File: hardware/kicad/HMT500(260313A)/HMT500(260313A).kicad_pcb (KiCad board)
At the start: 4 copper layers, 56.5 x 23 mm, 110 parts, among them J1 SM08B-GHS-TB, J2 TC2030-IDC-NL, J3 SM04B-SRSS-TB, J5 CHASSIS wire, U1 TPS26600PWPR, U10 TPS26611DDFR, U11 THVD2410DGKR, U12 OPA197IDBVR, U13 OPA197IDBVR, U14 SN74LVC2G32DCUR, U15 LMR51606YFDBVR, U2 LMR51606YFDBVR, U3 TPS7A2033PDBVR, U4 STM32G0B1CCT6, U5 PCAP04-AQFM-24, U6 ADS1220IPWR, U7 DAC8760IPWP, U8 DAC8760IPWP, U9 TPS26611DDFR

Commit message: 회로 v0.10: AO D30/D40을 TVS1401 14 V로 변경
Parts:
- D30, D40: value TVS3301DRBR -> TVS1401DRBR

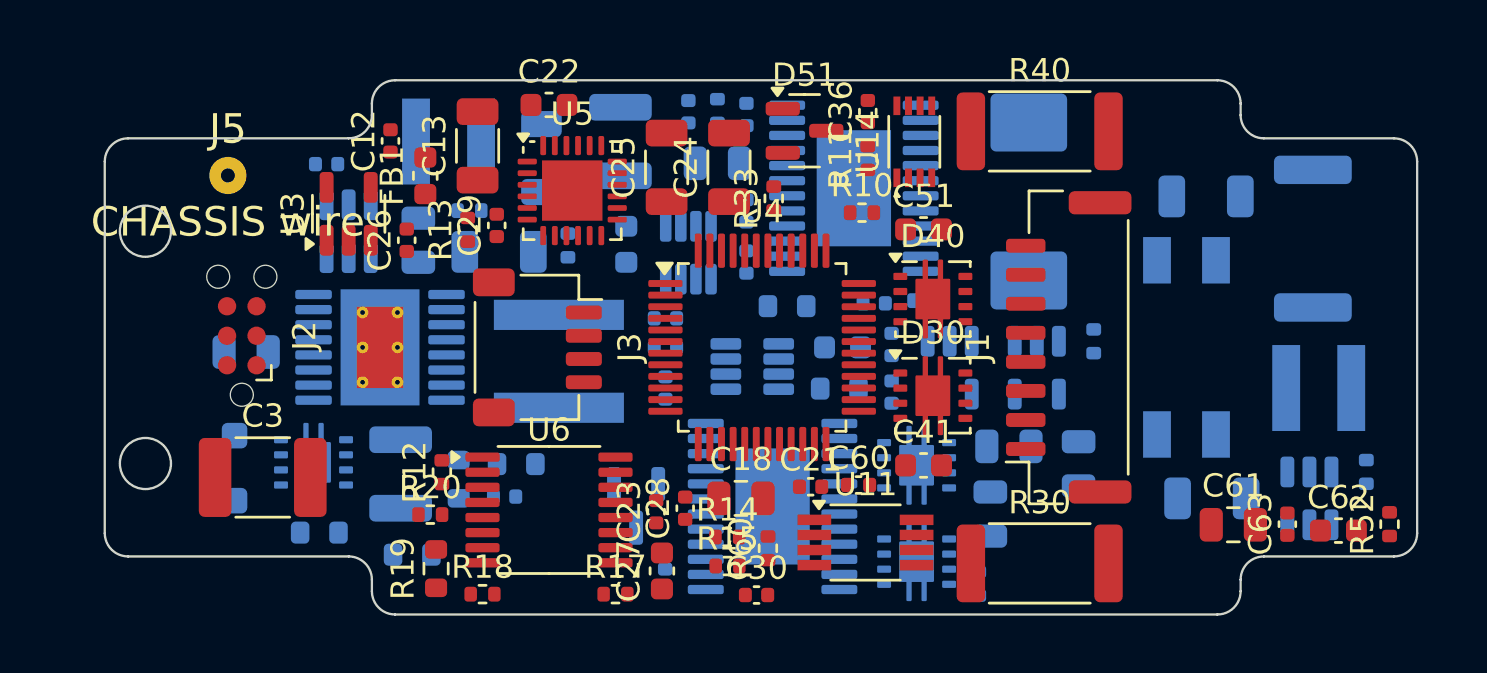
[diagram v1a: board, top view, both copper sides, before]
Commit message: Add HMT500 A1 routing draft and correct SMNR4020 land patterns
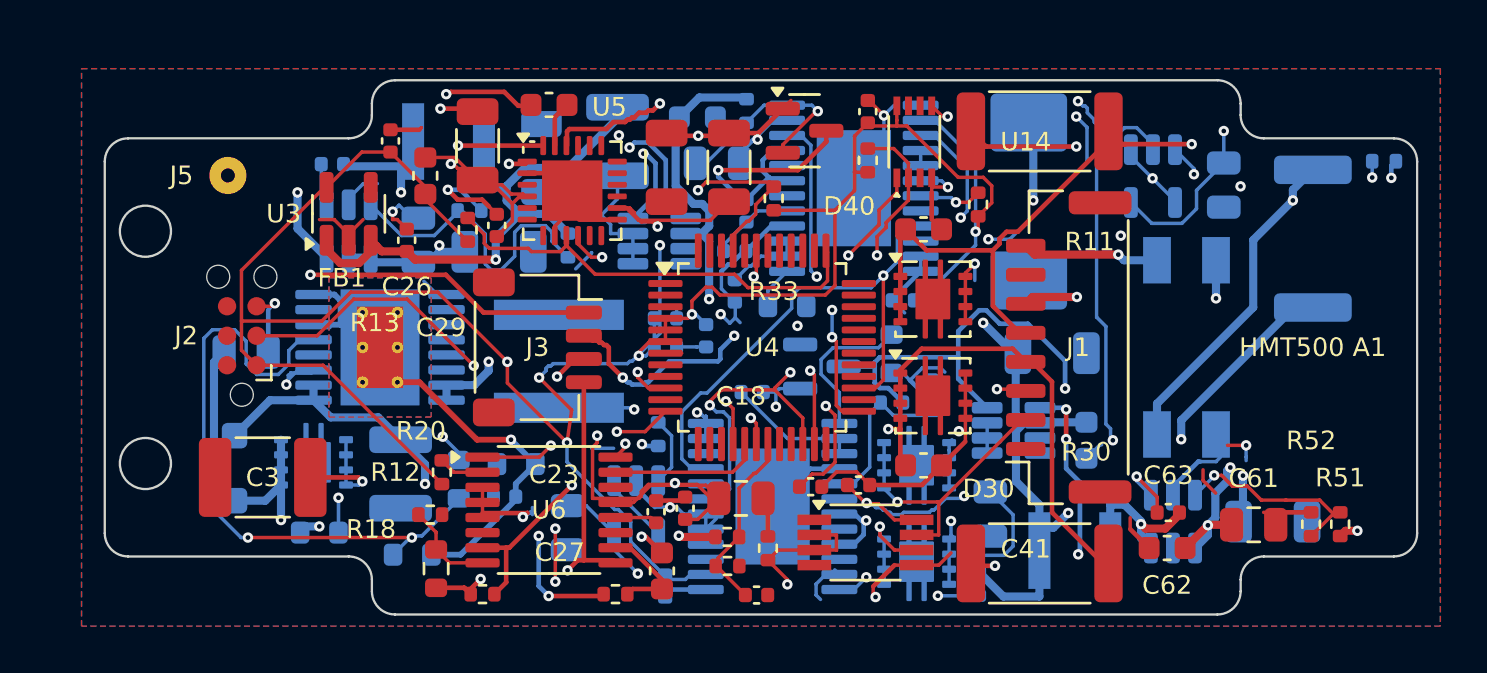
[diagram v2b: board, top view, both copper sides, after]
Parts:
- C1, C16, C18, C42, C45, C52, C55, C61: footprint Capacitor_SMD:C_0805_2012Metric -> HMT500_260313A:C_0805_2012Metric
- C12, C14, C15, C20, C21, C23, C26, C28, C29, C30, C36, C4, C40, C44, C47, C48, C50, C54, C57, C58, C60, C63, C8: footprint Capacitor_SMD:C_0402_1005Metric -> HMT500_260313A:C_0402_1005Metric
- C13, C24, C25, C5, C64, C65: footprint Capacitor_SMD:C_1206_3216Metric -> HMT500_260313A:C_1206_3216Metric
- C2, C6: footprint Capacitor_SMD:C_1210_3225Metric -> HMT500_260313A:C_1210_3225Metric
- C22, C27, C41, C46, C51, C56, C62: footprint Capacitor_SMD:C_0603_1608Metric -> HMT500_260313A:C_0603_1608Metric
- C3: footprint Capacitor_SMD:C_1812_4532Metric -> HMT500_260313A:C_1812_4532Metric
- D1: footprint Diode_SMD:D_SMC -> HMT500_260313A:D_SMC
- D3: footprint Diode_SMD:D_SOD-123F -> HMT500_260313A:D_SOD-123F
- D41, D51: footprint Package_TO_SOT_SMD:SOT-23 -> HMT500_260313A:SOT-23
- FB1: footprint Inductor_SMD:L_0603_1608Metric -> HMT500_260313A:L_0603_1608Metric
- J1: footprint Connector_JST:JST_GH_SM08B-GHS-TB_1x08-1MP_P1.25mm_Horizontal -> HMT500_260313A:JST_GH_SM08B-GHS-TB_1x08-1MP_P1.25mm_Horizontal
- J2: footprint Connector:Tag-Connect_TC2030-IDC-NL_2x03_P1.27mm_Vertical -> HMT500_260313A:Tag-Connect_TC2030-IDC-NL_2x03_P1.27mm_Vertical
- J3: footprint Connector_JST:JST_SH_SM04B-SRSS-TB_1x04-1MP_P1.00mm_Horizontal -> HMT500_260313A:JST_SH_SM04B-SRSS-TB_1x04-1MP_P1.00mm_Horizontal
- L1: footprint Inductor_SMD:L_CommonMode_Wuerth_WE-SL2 -> HMT500_260313A:L_CommonMode_Wuerth_WE-SL2
- L2, L3: footprint Inductor_SMD:L_Taiyo-Yuden_NR-40xx -> HMT500_260313A:L_SXN_SMNR4020
- R1, R30, R40: footprint Resistor_SMD:R_2512_6332Metric -> HMT500_260313A:R_2512_6332Metric
- R10, R11, R12, R13, R14, R15, R17, R18, R20, R31, R33, R34, R41, R44, R52, R60, R8, R9: footprint Resistor_SMD:R_0402_1005Metric -> HMT500_260313A:R_0402_1005Metric
- R19, R3, R32, R4, R42, R5, R6: footprint Resistor_SMD:R_0603_1608Metric -> HMT500_260313A:R_0603_1608Metric
- R2: footprint Resistor_SMD:R_1206_3216Metric -> HMT500_260313A:R_1206_3216Metric
- R51: footprint Resistor_SMD:R_0402_1005Metric -> HMT500_260313A:R_0402_1005Metric; moved to F.Cu
- U1: footprint Package_SO:HTSSOP-16-1EP_4.4x5mm_P0.65mm_EP3.4x5mm_Mask2.46x2.31mm_ThermalVias -> HMT500_260313A:HTSSOP-16-1EP_4.4x5mm_P0.65mm_EP3.4x5mm_Mask2.46x2.31mm_ThermalVias
- U10, U9: footprint Package_TO_SOT_SMD:SOT-23-8 -> HMT500_260313A:SOT-23-8
- U11: footprint Package_SO:VSSOP-8_3.0x3.0mm_P0.65mm -> HMT500_260313A:VSSOP-8_3.0x3.0mm_P0.65mm
- U12, U13, U3: footprint Package_TO_SOT_SMD:SOT-23-5 -> HMT500_260313A:SOT-23-5
- U14: footprint Package_SO:VSSOP-8_2.3x2mm_P0.5mm -> HMT500_260313A:VSSOP-8_2.3x2mm_P0.5mm
- U15, U2: footprint Package_TO_SOT_SMD:SOT-23-6 -> HMT500_260313A:SOT-23-6
- U4: footprint Package_QFP:LQFP-48_7x7mm_P0.5mm -> HMT500_260313A:LQFP-48_7x7mm_P0.5mm
- U5: footprint Package_DFN_QFN:QFN-24-1EP_4x4mm_P0.5mm_EP2.6x2.6mm -> HMT500_260313A:QFN-24-1EP_4x4mm_P0.5mm_EP2.6x2.6mm
- U6: footprint Package_SO:TSSOP-16_4.4x5mm_P0.65mm -> HMT500_260313A:TSSOP-16_4.4x5mm_P0.65mm
- U7, U8: footprint Package_SO:HTSSOP-24-1EP_4.4x7.8mm_P0.65mm_EP3.2x5mm -> HMT500_260313A:HTSSOP-24-1EP_4.4x7.8mm_P0.65mm_EP3.2x5mm
- moved C45 19.3 mm to (119.9, 107.8), turned to -90 degrees
- moved U12 14.8 mm to (122.9, 106.9)
- moved R41 14.7 mm to (155.1, 92.0), turned to 0 degrees
- moved C55 13.5 mm to (148.2, 93.0)
- moved R31 12.9 mm to (123.8, 103.7), turned to -90 degrees
- moved L3 12.6 mm to (141.8, 108.8), turned to 180 degrees
- moved U9 11.6 mm to (139.1, 103.6)
- moved C46 11.2 mm to (142.3, 104.0), turned to -90 degrees
- moved C54 10.5 mm to (134.4, 98.0), turned to 180 degrees
- moved D41 10.0 mm to (130.9, 100.8), turned to 0 degrees
- moved U13 9.65 mm to (145.1, 92.6)
- moved C65 9.46 mm to (140.8, 100.2)
- moved C62 7.41 mm to (145.7, 108.6), turned to 180 degrees
- moved C58 6.32 mm to (127.1, 95.9), turned to 0 degrees
- moved C56 6.26 mm to (125.5, 90.1), turned to 0 degrees
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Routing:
- net +3V3: track 0.00 -> 200.0 mm, vias 0 -> 13
- net GND: track 0.00 -> 145.7 mm, vias 0 -> 24
- net VIN_P: track 0.00 -> 71.2 mm, vias 0 -> 5
- net VIN_F: track 0.00 -> 62.9 mm, vias 0 -> 2
- net VAO: track 0.00 -> 62.6 mm, vias 0 -> 5
- net DAC1_LATCH: track 0.00 -> 35.1 mm, vias 0 -> 3
- net OUT2_EXT: track 0.00 -> 34.0 mm, vias 0 -> 2
- net DAC2_AVDD: track 0.00 -> 34.0 mm, vias 0 -> 2
- net RS485_DE: track 0.00 -> 33.9 mm, vias 0 -> 4
- net NRST: track 0.00 -> 33.5 mm, vias 0 -> 3
- net DAC1_OUT: track 0.00 -> 33.2 mm, vias 0 -> 2
- net OUT1_EXT: track 0.00 -> 32.8 mm, vias 0 -> 2
- net DAC_SCK: track 0.00 -> 32.6 mm, vias 0 -> 6
- net +3V3A: track 0.00 -> 30.7 mm, vias 0 -> 2
- net OUT2_P: track 0.00 -> 30.3 mm, vias 0 -> 2
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- added copper zone on B.Cu, net EF_RTN
- added copper zone on F.Cu, net EF_RTN
- added copper zone on B.Cu, net GND
- added copper zone on F.Cu, net GND
- added copper zone on In1.Cu, net GND
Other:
- board text added: "HMT500 A1"

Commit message: Save HMT500 A2 layout improvements as an incomplete routing draft
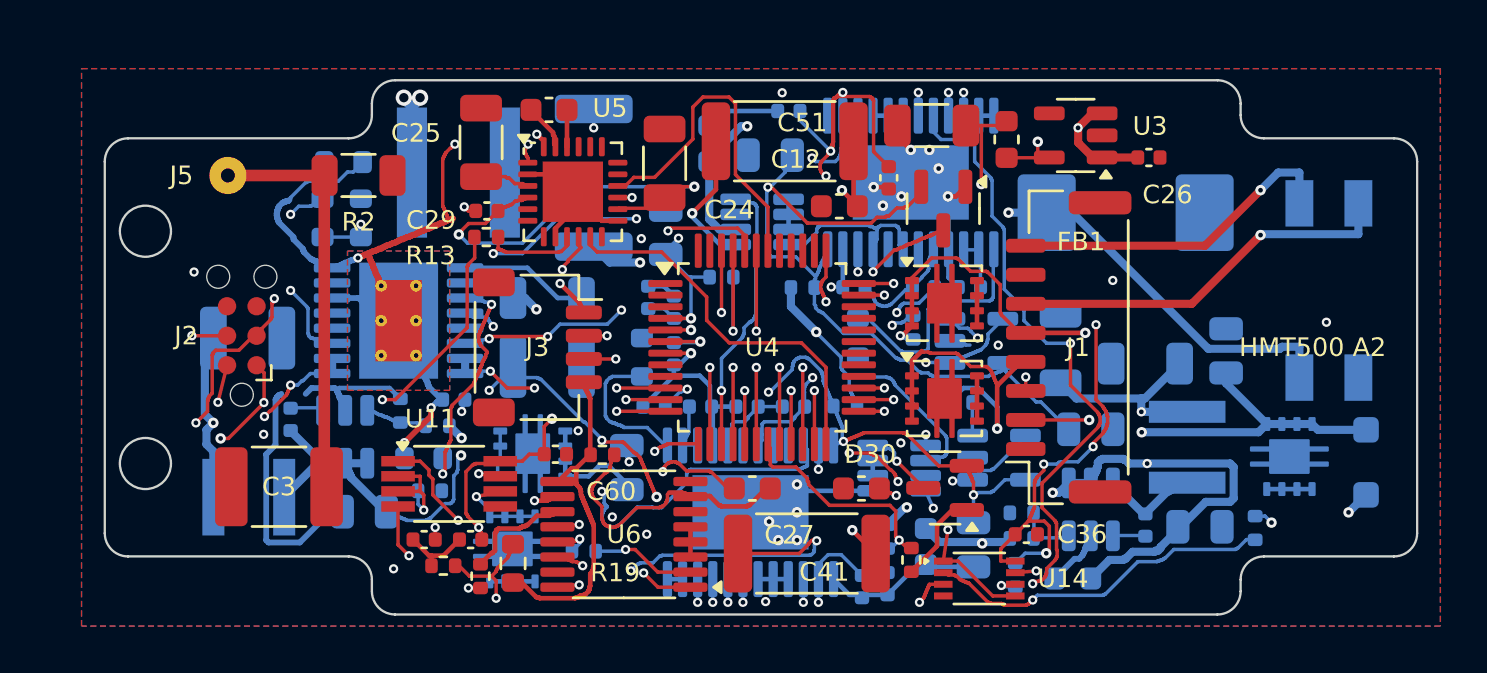
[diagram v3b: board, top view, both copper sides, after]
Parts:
- C18, C21, C30, C61, C62, C63, R10, R11, R12, R14, R33, R51, R52, R60: moved to B.Cu
- D41, R2: moved to F.Cu
- moved D3 48.7 mm to (154.3, 105.0), turned to 90 degrees
- moved C1 42.2 mm to (148.3, 100.2), turned to 90 degrees
- moved D2 42.0 mm to (151.0, 104.7), turned to -90 degrees
- moved C26 32.1 mm to (144.9, 91.8), turned to 0 degrees
- moved U3 31.5 mm to (141.8, 90.9), turned to 180 degrees
- moved R1 31.1 mm to (121.0, 92.7)
- moved FB1 25.1 mm to (138.8, 91.0)
- moved R10 23.0 mm to (149.5, 107.8), turned to -90 degrees
- moved C12 21.5 mm to (133.8, 92.7), turned to -90 degrees
- moved R41 21.5 mm to (134.8, 99.2), turned to -90 degrees
- moved C13 19.6 mm to (135.6, 90.5), turned to 180 degrees
- moved C36 19.4 mm to (139.7, 108.0), turned to 0 degrees
- moved U14 19.0 mm to (137.7, 110.0), turned to 0 degrees
- moved U11 18.1 mm to (114.8, 105.9)
- moved C6 18.0 mm to (106.2, 99.6), turned to 0 degrees
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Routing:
- net VIN_D: track 17.7 -> 69.4 mm, vias 2 -> 7
- net GND: track 145.7 -> 98.8 mm, vias 24 -> 28
- net +3V3: track 200.0 -> 156.5 mm, vias 13 -> 20
- net +5V: track 24.5 -> 64.0 mm, vias 1 -> 3
- net OUT1_P: track 12.5 -> 48.3 mm, vias 4 -> 3
- net DAC2_SCLK: track 0.00 -> 33.2 mm, vias 0 -> 3
- net CHASSIS: track 0.00 -> 33.1 mm, vias 0 -> 2
- net DAC1_SENSE: track 3.06 -> 32.9 mm, vias 0 -> 2
- net VIN_P: track 71.2 -> 99.4 mm, vias 5 -> 7
- net RS485_B_EXT: track 12.1 -> 40.2 mm, vias 1 -> 2
- net OV_DIV: track 27.6 -> 0.00 mm, vias 2 -> 0
- net OUT2_P: track 30.3 -> 6.04 mm, vias 2 -> 1
- net VAO: track 62.6 -> 84.0 mm, vias 5 -> 4
- net DAC_MOSI: track 23.5 -> 3.10 mm, vias 1 -> 3
- net EF_RTN: track 26.6 -> 46.0 mm, vias 1 -> 4
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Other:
- board text added: "HMT500 A2"
- board text removed: "HMT500 A1"

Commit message: Adopt six-layer A3 draft with 0.15 mm signal vias
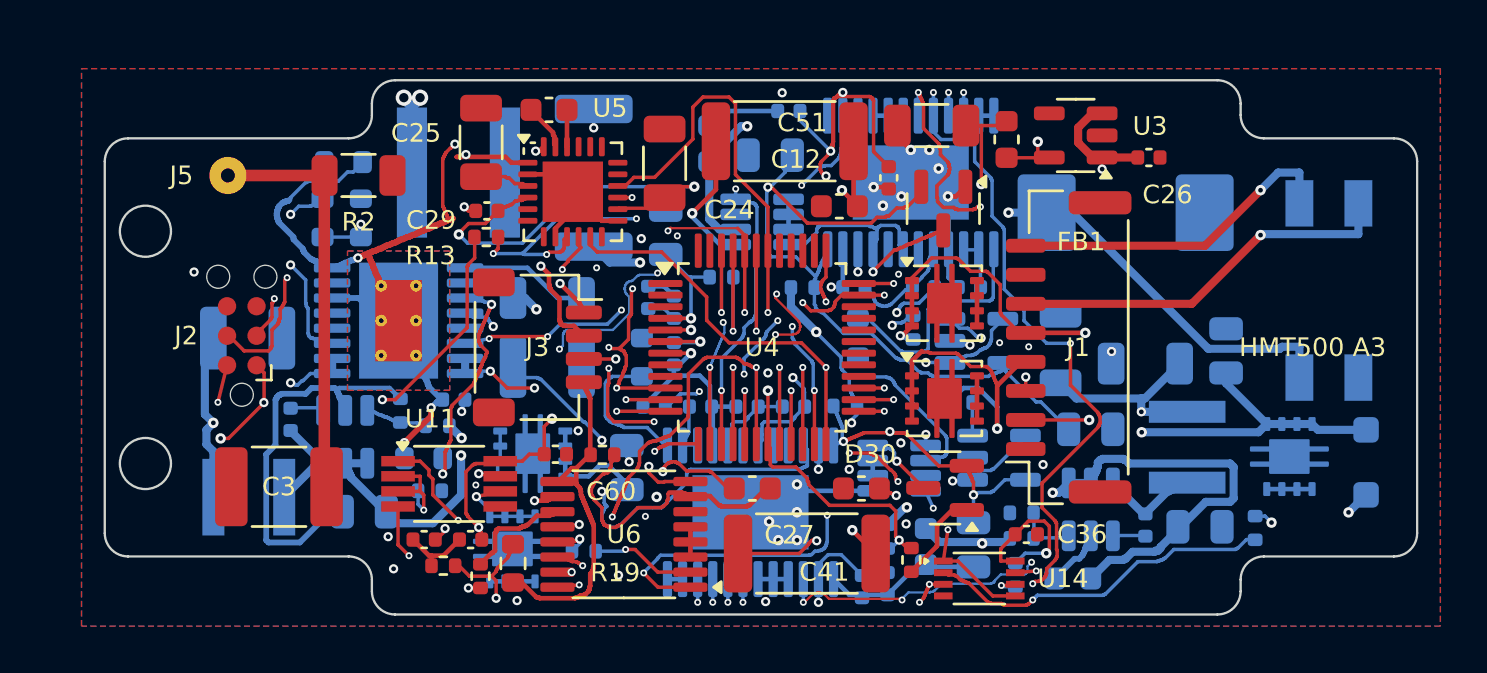
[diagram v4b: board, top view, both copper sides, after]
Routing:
- net DAC_MISO: track 3.50 -> 58.8 mm, vias 3 -> 5
- net DAC_MOSI: track 3.10 -> 53.0 mm, vias 3 -> 4
- net VIN_P: track 99.4 -> 49.8 mm, vias 7 -> 6
- net DAC2_LATCH: track 4.55 -> 44.5 mm, vias 3 -> 5
- net SWDIO: track 2.74 -> 41.6 mm, vias 2 -> 4
- net OUT1_P: track 48.3 -> 12.5 mm
- net DAC_ALARM: track 34.1 -> 65.0 mm, vias 3 -> 7
- net RS485_RX: track 7.48 -> 37.1 mm, vias 2 -> 7
- net DAC1_LATCH: track 19.8 -> 43.9 mm
- net +3V3A: track 37.8 -> 59.8 mm, vias 5 -> 6
- net RS485_TX: track 4.34 -> 25.3 mm, vias 2 -> 5
- net +3V3: track 156.5 -> 138.2 mm, vias 20 -> 16
- net REF_N: track 4.61 -> 20.4 mm, vias 1 -> 2
- net ADC_DRDY: track 3.57 -> 15.9 mm
- net SPI_SCK: track 19.2 -> 30.9 mm, vias 4 -> 5
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- added copper zone on In4.Cu, net GND
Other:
- copper layers 4 -> 6
- board text added: "HMT500 A3"
- board text removed: "HMT500 A2"

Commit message: HMT500 A4: improve six-layer routing; five connections remain
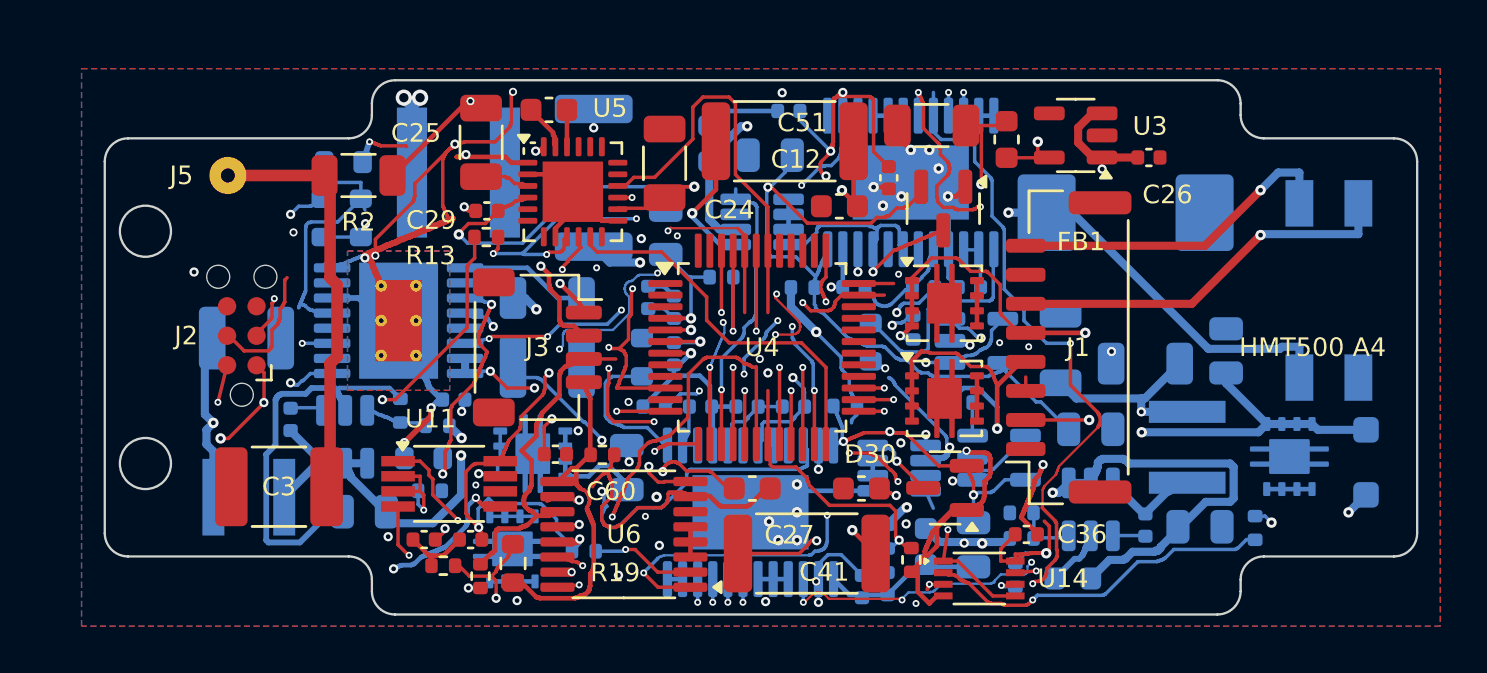
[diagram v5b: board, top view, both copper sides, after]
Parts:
- moved R42 0.59 mm to (133.0, 99.8)
- moved C6 0.05 mm to (106.1, 99.6)
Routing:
- net +3V3: track 138.2 -> 166.7 mm, vias 16 -> 19
- net GND: track 99.9 -> 125.6 mm, vias 27 -> 31
- net SPI_MISO: track 2.91 -> 18.2 mm
- net EF_RTN: track 46.0 -> 60.4 mm, vias 4 -> 8
- net VAO: track 84.8 -> 95.8 mm, vias 5 -> 6
- net OV_DIV: track 0.00 -> 11.0 mm
- net PT_P: track 6.23 -> 15.0 mm, vias 1 -> 0
- net DAC_MOSI: track 53.0 -> 55.5 mm, vias 4 -> 6
- net RS485_A_EXT: track 4.69 -> 2.83 mm, vias 2 -> 0
- net OUT1_SGOOD: track 2.52 -> 0.82 mm, vias 2 -> 0
- net SWDIO: track 41.6 -> 43.0 mm, vias 4 -> 3
- net DAC1_LATCH: track 43.9 -> 44.8 mm
- net CHASSIS: track 33.1 -> 33.8 mm
- net PT_SN_F: track 12.5 -> 13.1 mm
- net DAC2_ISET: track 10.6 -> 11.1 mm
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- added copper zone on In2.Cu, net +3V3
- added copper zone on In3.Cu, net +3V3
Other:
- board text added: "HMT500 A4"
- board text removed: "HMT500 A3"
